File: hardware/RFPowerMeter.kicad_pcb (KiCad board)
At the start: 2 copper layers, 100 x 100 mm, 40 parts, among them IC1 ATMEGA328-P, P1 SMA, P2 SMA, P3 CONN_01X01, P4 CONN_01X01, SW1 SELECT, U1 7805, U2 AD8307, U3 4056, U4 4056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

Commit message: Improved noise immunity
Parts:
- removed P1, P2: SMA, Pin_Headers:Pin_Header_Straight_1x02
- added C14: 100µF, Capacitors_ThroughHole:C_Radial_D6.3_L11.2_P2.5, F.Cu at (90.9, 87.6)
- added GND: SolderWirePad_single_1-2mmDrill, Wire_Pads:SolderWirePad_single_1-2mmDrill, F.Cu at (120.9, 141.5)
- added REF**: RF shield, Mounting_Holes:MountingHole_2-5mm, B.Cu at (111.3, 138.9)
- added REF**: RF shield, Mounting_Holes:MountingHole_2-5mm, F.Cu at (111.3, 118.6)
- R3: footprint Resistors_ThroughHole:Resistor_Horizontal_RM15mm -> Wire_Pads:SolderWirePad_single_1-2mmDrill
- moved RV1 18.1 mm to (114.0, 124.0), turned to 0 degrees
- moved C4 18.1 mm to (117.6, 132.6), turned to 270 degrees
- moved C6 15.6 mm to (125.2, 122.2), turned to 0 degrees
- moved R3 14.2 mm to (117.6, 141.5), turned to 0 degrees
- moved R8 12.8 mm to (139.4, 123.7)
- moved R5 11.7 mm to (136.7, 133.9), turned to 90 degrees
- moved C11 11.2 mm to (130.3, 135.6)
- moved C7 11.2 mm to (125.2, 135.6)
- moved U2 11.0 mm to (125.2, 132.6)
- moved R4 9.57 mm to (121.4, 125.5)
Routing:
- net +5V: track 288.0 -> 369.7 mm
- net MEAS: track 59.8 -> 71.9 mm
- net Net-(C4-Pad2): track 14.8 -> 6.39 mm
- net 7-13.8V: track 22.6 -> 30.4 mm
- net Net-(C4-Pad1): track 13.9 -> 20.9 mm
- net Net-(P1-Pad1): track 6.60 -> 0.00 mm
- net /M2: track 100.2 -> 95.4 mm
- net Net-(R4-Pad1): track 10.8 -> 6.51 mm
- net Net-(C6-Pad2): track 18.1 -> 13.9 mm
- net /ENB: track 45.6 -> 47.3 mm
- net Net-(C11-Pad2): track 12.8 -> 11.2 mm
- net Net-(C7-Pad1): track 8.40 -> 6.86 mm
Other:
- board text added: "V1.1"
- board text removed: "V1.0"

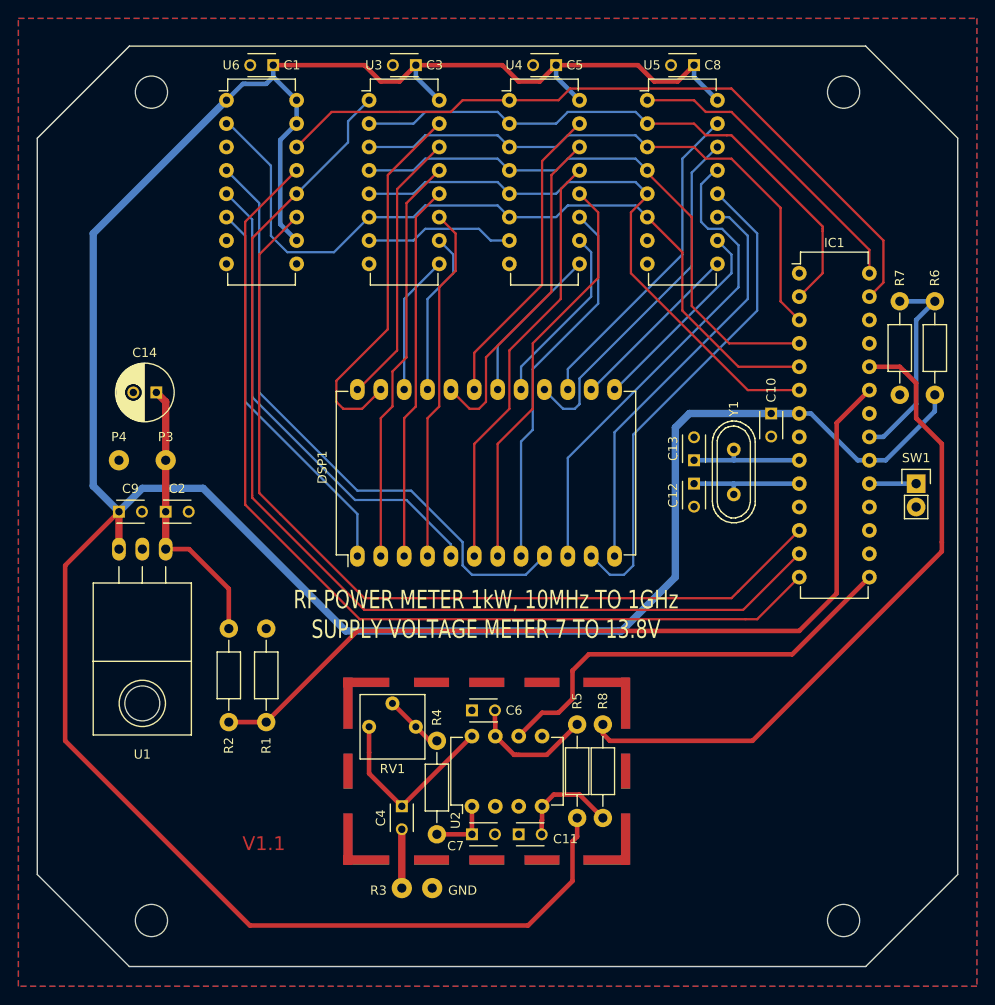
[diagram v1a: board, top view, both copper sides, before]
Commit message: Improved noice immunity, fixed hole sizes
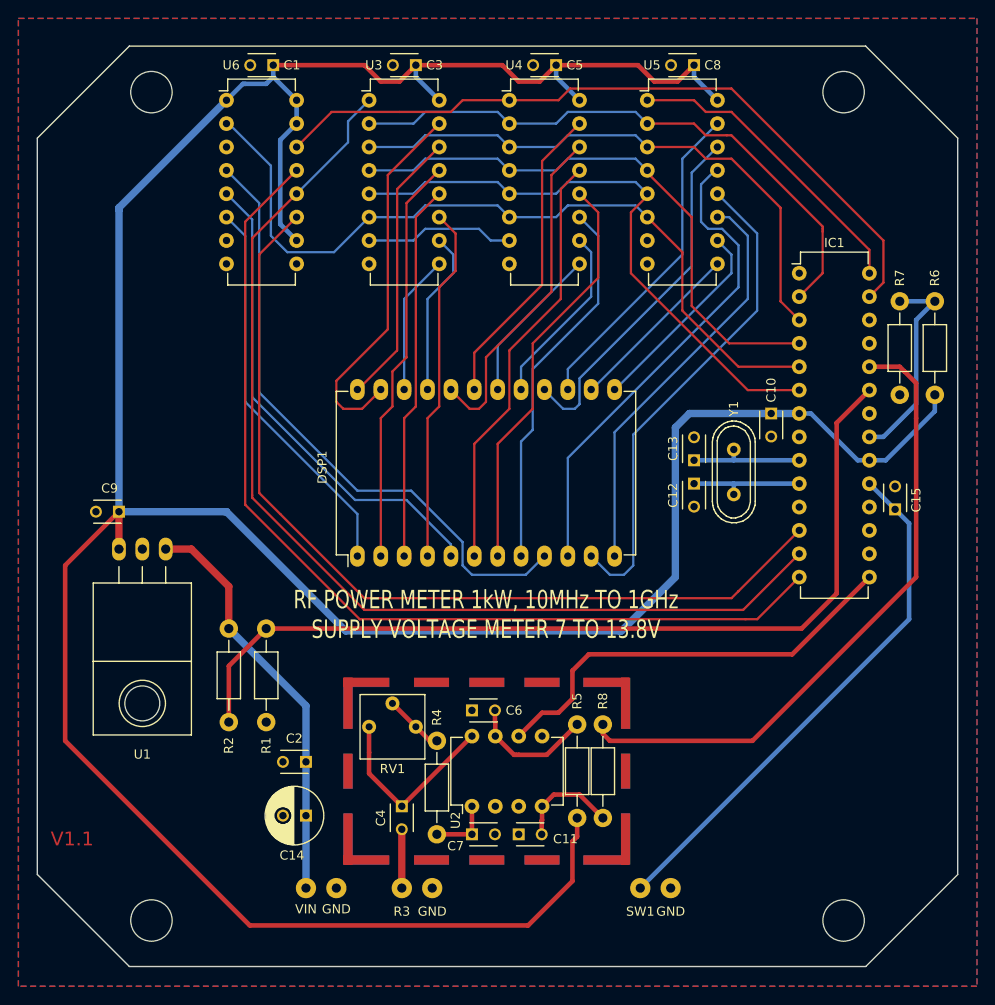
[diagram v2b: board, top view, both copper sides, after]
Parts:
- removed the REF** at (165.6, 145.0)
- removed the REF** at (90.4, 145.0)
- removed the REF** at (90.4, 55.0)
- removed the REF** at (165.6, 55.0)
- added C15: 100nF, Capacitors_ThroughHole:C_Disc_D3_P2.5, F.Cu at (171.2, 100.3)
- added GND: SolderWirePad_single_1-2mmDrill, Wire_Pads:SolderWirePad_single_1-2mmDrill, F.Cu at (146.8, 141.5)
- added REF**: MountingHole_4-5mm, Mounting_Holes:MountingHole_4-5mm, F.Cu at (90.4, 145.0)
- added REF**: MountingHole_4-5mm, Mounting_Holes:MountingHole_4-5mm, F.Cu at (165.6, 145.0)
- added REF**: MountingHole_4-5mm, Mounting_Holes:MountingHole_4-5mm, F.Cu at (165.6, 55.0)
- added REF**: MountingHole_4-5mm, Mounting_Holes:MountingHole_4-5mm, F.Cu at (90.4, 55.0)
- SW1: footprint Pin_Headers:Pin_Header_Straight_1x02 -> Wire_Pads:SolderWirePad_single_0-8mmDrill
- moved SW1 53.2 mm to (143.5, 141.5), turned to 270 degrees
- moved GND 52.1 mm to (110.5, 141.5)
- moved VIN 48.9 mm to (107.2, 141.5)
- moved C14 48.8 mm to (107.2, 133.6)
- moved C2 31.2 mm to (107.2, 127.8), turned to 180 degrees
- moved R2 10.2 mm to (102.9, 113.3), turned to 270 degrees
- turned C9 to 180 degrees
- renumbered P4 to GND, P3 to VIN
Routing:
- net Net-(C15-Pad1): track 5.08 -> 57.8 mm
- net 7-13.8V: track 30.4 -> 44.8 mm
- net +5V: track 369.7 -> 366.0 mm
- net /M2: track 95.4 -> 99.0 mm
- net MEAS: track 71.9 -> 69.6 mm
